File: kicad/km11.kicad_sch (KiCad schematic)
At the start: 8 parts, among them J1 DEC-FLIP-CHIP_CONN-DEC-DOUBLE, U1 ATtiny1616-S, U2 PCF8574T, U3 PCF8574T, U4 PCF8574T, U5 PCF8574T, U6 PCF8574T, U7 PCF8574T

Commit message: First small parts
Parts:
- added C1, C2, C3, C4, C5, C6, C7: 100nF, Capacitor_SMD:C_0805_2012Metric, symbol Device:C
- added C8: 100uF, Capacitor_SMD:CP_Elec_6.3x7.7, symbol Device:C_Polarized
- added J2: Conn_02x10_Odd_Even, Connector_PinHeader_2.54mm:PinHeader_2x10_P2.54mm_Vertical, symbol Connector_Generic:Conn_02x10_Odd_Even
- added R1, R2: 4.7k, Resistor_SMD:R_0805_2012Metric, symbol Device:R
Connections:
- net GND: now reaches U4.1 (A0)
- net GND: now also U1.20 (GND), U2.1 (A0), U2.2 (A1), U2.3 (A2), U2.8 (GND), U3.2 (A1), U3.3 (A2), U3.8 (GND), U4.3 (A2), U4.8 (GND), U5.3 (A2), U5.8 (GND), U6.1 (A0), U6.2 (A1), U6.8 (GND), U7.2 (A1), U7.8 (GND), C1.2, C2.2, C3.2, C4.2, C5.2, C6.2, C7.2, C8.2, J2.1 (Pin_1), J2.2 (Pin_2)
- net SCL: now reaches U4.14 (SCL)
- net SCL: now also U1.11 (PB0), U2.14 (SCL), U3.14 (SCL), U5.14 (SCL), U6.14 (SCL), U7.14 (SCL), R2.2
- net SDA: now reaches U4.15 (SDA)
- net SDA: now also U1.10 (PB1), U2.15 (SDA), U3.15 (SDA), U5.15 (SDA), U6.15 (SDA), U7.15 (SDA), R1.2
- net +5V: now reaches U4.16 (VDD)
- net +5V: now also U1.1 (VCC), U2.16 (VDD), U3.1 (A0), U3.16 (VDD), U4.2 (A1), U5.1 (A0), U5.16 (VDD), U5.2 (A1), U6.16 (VDD), U6.3 (A2), U7.1 (A0), U7.16 (VDD), U7.3 (A2), C1.1, C2.1, C3.1, C4.1, C5.1, C6.1, C7.1, C8.1, J2.19 (Pin_19), J2.20 (Pin_20), R1.1, R2.1
- net MOSI: now reaches U1.17 (PA1)
- net MOSI: now also J2.4 (Pin_4)
- net MISO: now reaches U1.18 (PA2)
- net MISO: now also J2.6 (Pin_6)
- net SCK: now reaches U1.19 (PA3)
- net SCK: now also J2.8 (Pin_8)
- net SPI_SS: now reaches U1.2 (PA4)
- net SPI_SS: now also J2.10 (Pin_10)
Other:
- note added: "Decoupling: C1=U1 C2=U2 C3=U3 C4=U4 C5=U5 C6=U6 C7=U7 - place one adjacent to each IC's VDD pin on the PCB"

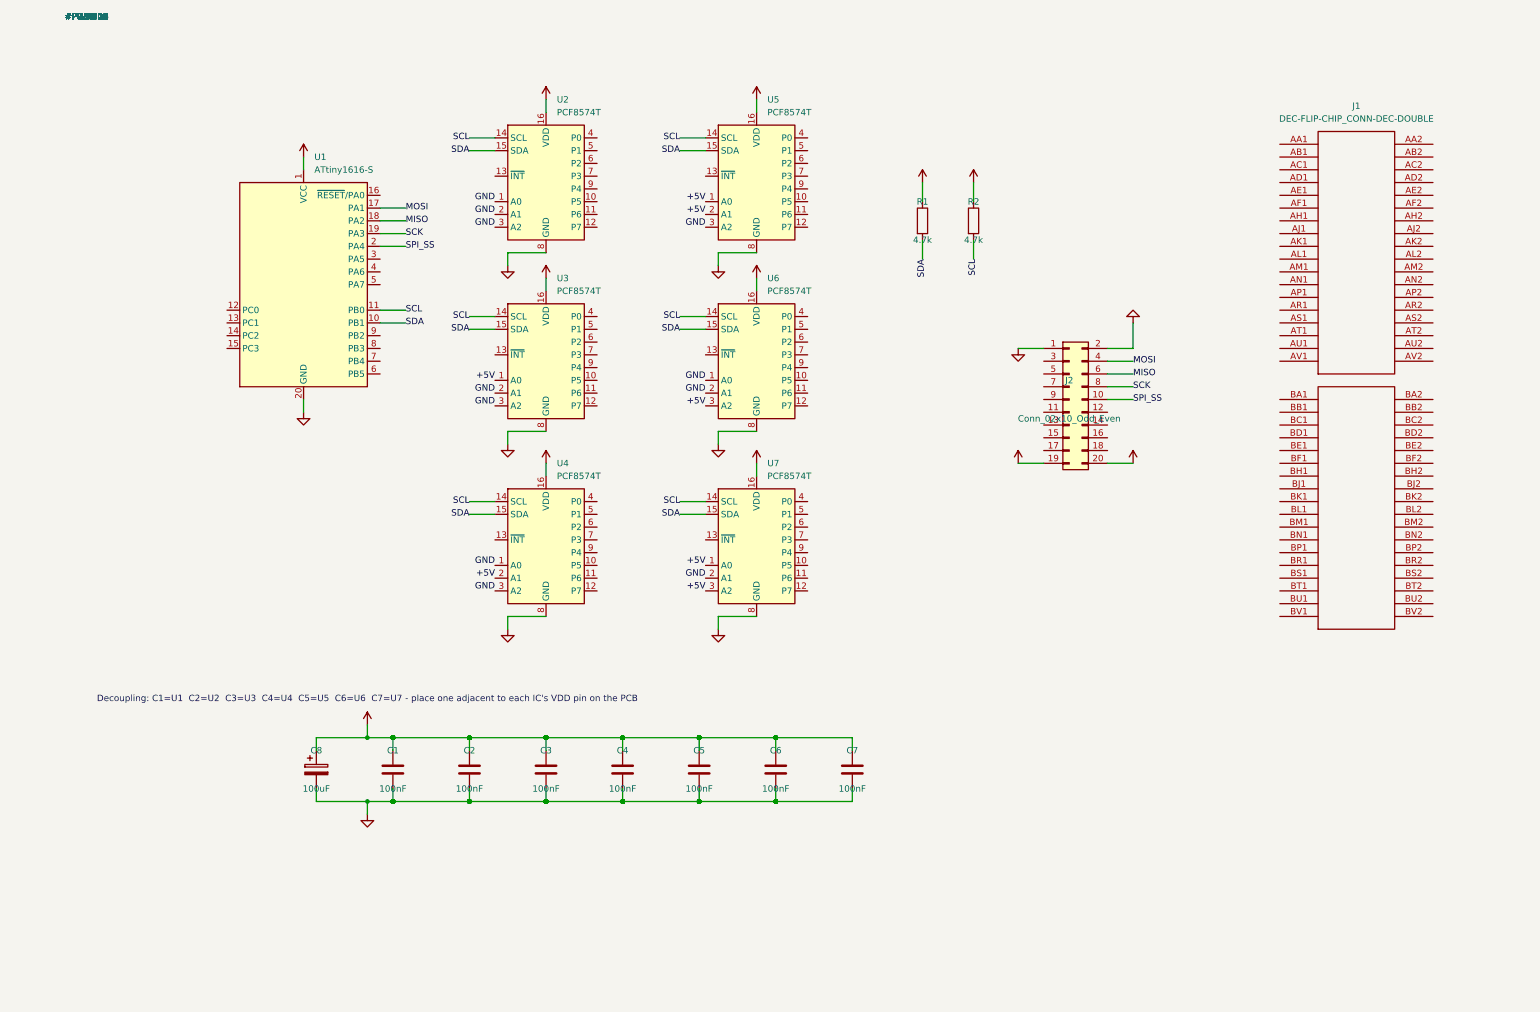
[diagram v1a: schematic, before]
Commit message: Add all flipchip signal names from Joergs sheet
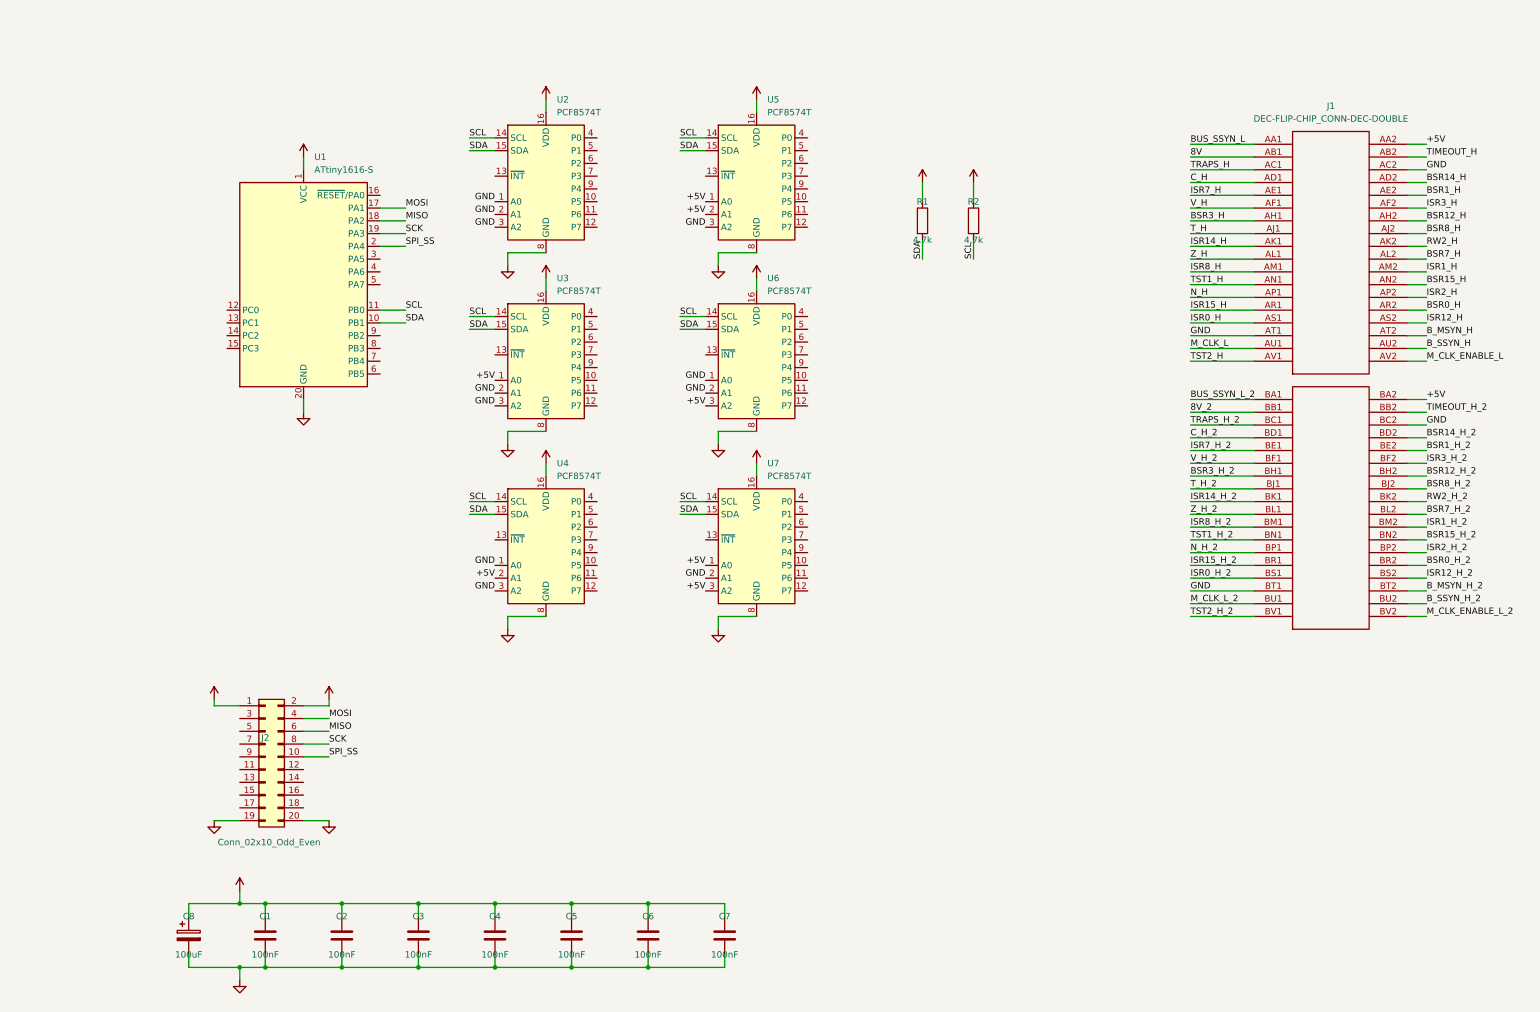
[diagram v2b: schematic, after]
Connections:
- net +5V: now also J1.AA2, J1.BA2, J2.1 (Pin_1), J2.2 (Pin_2); no longer J2.19 (Pin_19), J2.20 (Pin_20)
- net GND: now also J1.AC2, J1.AT1, J1.BC2, J1.BT1, J2.19 (Pin_19), J2.20 (Pin_20); no longer J2.1 (Pin_1), J2.2 (Pin_2)
- net BUS_SSYN_L: now reaches J1.AA1
- net 8V: now reaches J1.AB1
- net TIMEOUT_H: now reaches J1.AB2
- net TRAPS_H: now reaches J1.AC1
- net C_H: now reaches J1.AD1
- net BSR14_H: now reaches J1.AD2
- net ISR7_H: now reaches J1.AE1
- net BSR1_H: now reaches J1.AE2
- net V_H: now reaches J1.AF1
- net ISR3_H: now reaches J1.AF2
- net BSR3_H: now reaches J1.AH1
- net BSR12_H: now reaches J1.AH2
- net T_H: now reaches J1.AJ1
- net BSR8_H: now reaches J1.AJ2
- net ISR14_H: now reaches J1.AK1
- net RW2_H: now reaches J1.AK2
- net Z_H: now reaches J1.AL1
- net BSR7_H: now reaches J1.AL2
- net ISR8_H: now reaches J1.AM1
- net ISR1_H: now reaches J1.AM2
- net TST1_H: now reaches J1.AN1
- net BSR15_H: now reaches J1.AN2
- net N_H: now reaches J1.AP1
- net ISR2_H: now reaches J1.AP2
- net ISR15_H: now reaches J1.AR1
- net BSR0_H: now reaches J1.AR2
- net ISR0_H: now reaches J1.AS1
- net ISR12_H: now reaches J1.AS2
- net B_MSYN_H: now reaches J1.AT2
- net M_CLK_L: now reaches J1.AU1
- net B_SSYN_H: now reaches J1.AU2
- net TST2_H: now reaches J1.AV1
- net M_CLK_ENABLE_L: now reaches J1.AV2
- net BUS_SSYN_L_2: now reaches J1.BA1
- net 8V_2: now reaches J1.BB1
- net TIMEOUT_H_2: now reaches J1.BB2
- net TRAPS_H_2: now reaches J1.BC1
- net C_H_2: now reaches J1.BD1
- net BSR14_H_2: now reaches J1.BD2
- net ISR7_H_2: now reaches J1.BE1
- net BSR1_H_2: now reaches J1.BE2
- net V_H_2: now reaches J1.BF1
- net ISR3_H_2: now reaches J1.BF2
- net BSR3_H_2: now reaches J1.BH1
- net BSR12_H_2: now reaches J1.BH2
- net T_H_2: now reaches J1.BJ1
- net BSR8_H_2: now reaches J1.BJ2
- net ISR14_H_2: now reaches J1.BK1
- net RW2_H_2: now reaches J1.BK2
- net Z_H_2: now reaches J1.BL1
- net BSR7_H_2: now reaches J1.BL2
- net ISR8_H_2: now reaches J1.BM1
- net ISR1_H_2: now reaches J1.BM2
- net TST1_H_2: now reaches J1.BN1
- net BSR15_H_2: now reaches J1.BN2
- net N_H_2: now reaches J1.BP1
- net ISR2_H_2: now reaches J1.BP2
- net ISR15_H_2: now reaches J1.BR1
- net BSR0_H_2: now reaches J1.BR2
- net ISR0_H_2: now reaches J1.BS1
- net ISR12_H_2: now reaches J1.BS2
- net B_MSYN_H_2: now reaches J1.BT2
- net M_CLK_L_2: now reaches J1.BU1
- net B_SSYN_H_2: now reaches J1.BU2
- net TST2_H_2: now reaches J1.BV1
- net M_CLK_ENABLE_L_2: now reaches J1.BV2
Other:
- note removed: "Decoupling: C1=U1 C2=U2 C3=U3 C4=U4 C5=U5 C6=U6 C7=U7 - place one adjacent to each IC's VDD pin on the PCB"
- moved on the sheet: C1, C2, C3, C4, C5, C6, C7, C8, J1, J2

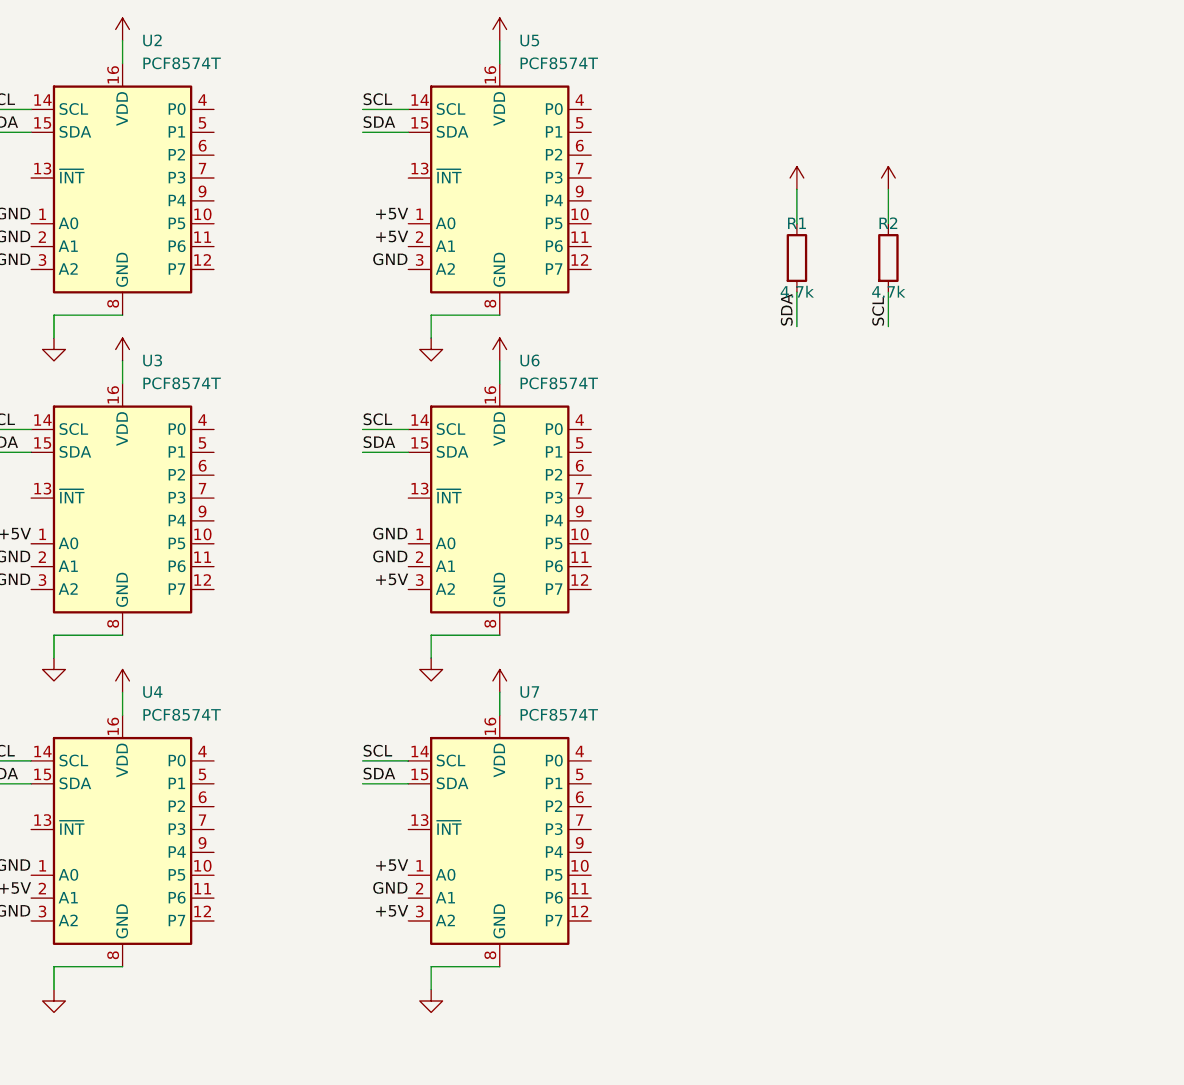
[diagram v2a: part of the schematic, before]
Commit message: All ports assigned
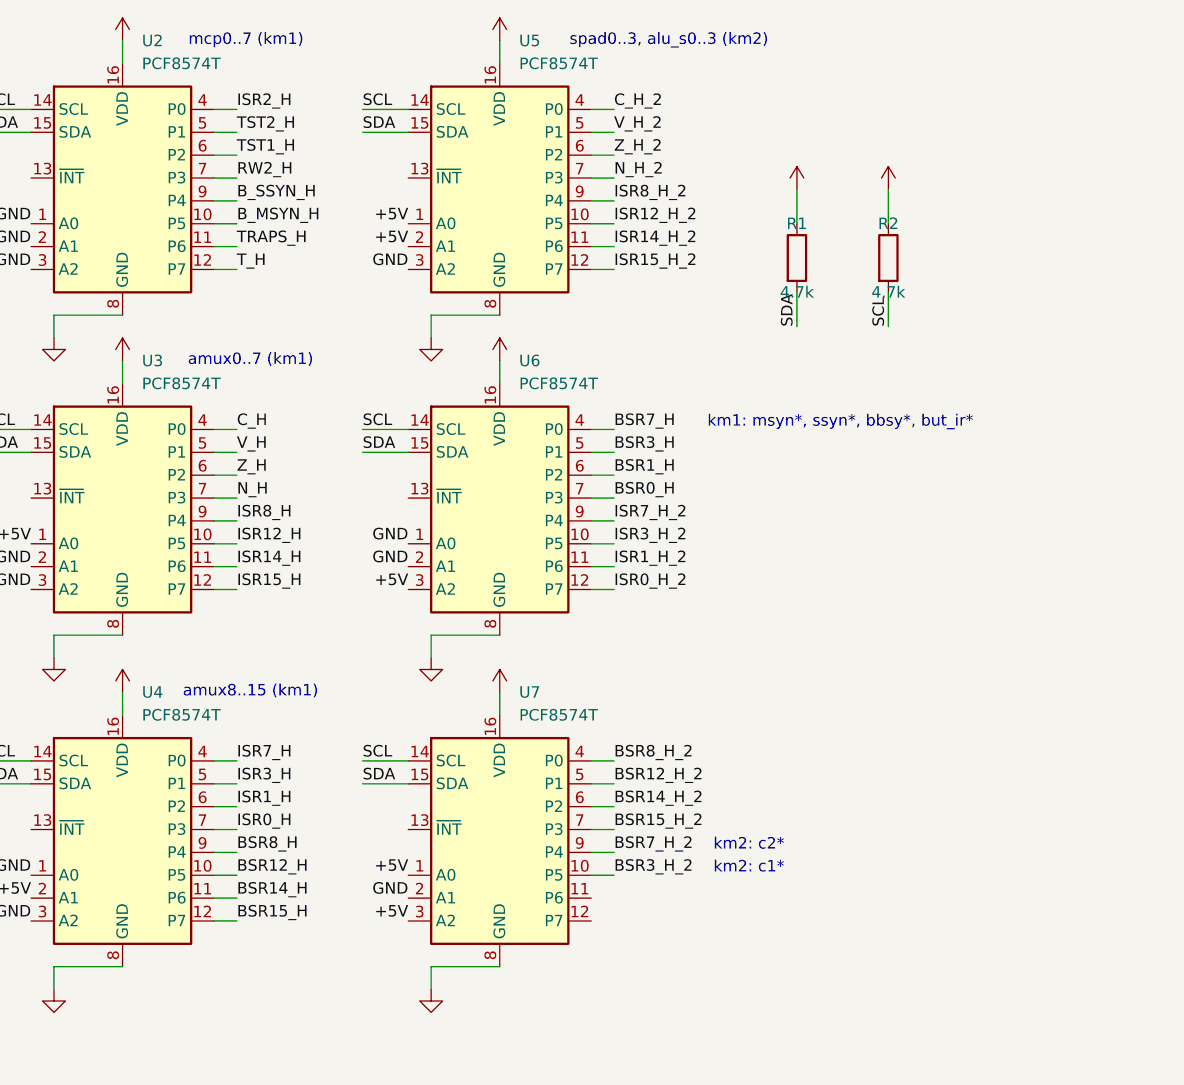
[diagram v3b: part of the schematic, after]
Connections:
- net BSR0_H: now also U6.7 (P3)
- net BSR12_H: now also U4.10 (P5)
- net BSR12_H_2: now also U7.5 (P1)
- net BSR14_H: now also U4.11 (P6)
- net BSR14_H_2: now also U7.6 (P2)
- net BSR15_H: now also U4.12 (P7)
- net BSR15_H_2: now also U7.7 (P3)
- net BSR1_H: now also U6.6 (P2)
- net BSR3_H: now also U6.5 (P1)
- net BSR3_H_2: now also U7.10 (P5)
- net BSR7_H: now also U6.4 (P0)
- net BSR7_H_2: now also U7.9 (P4)
- net BSR8_H: now also U4.9 (P4)
- net BSR8_H_2: now also U7.4 (P0)
- net B_MSYN_H: now also U2.10 (P5)
- net B_SSYN_H: now also U2.9 (P4)
- net C_H: now also U3.4 (P0)
- net C_H_2: now also U5.4 (P0)
- net ISR0_H: now also U4.7 (P3)
- net ISR0_H_2: now also U6.12 (P7)
- net ISR12_H: now also U3.10 (P5)
- net ISR12_H_2: now also U5.10 (P5)
- net ISR14_H: now also U3.11 (P6)
- net ISR14_H_2: now also U5.11 (P6)
- net ISR15_H: now also U3.12 (P7)
- net ISR15_H_2: now also U5.12 (P7)
- net ISR1_H: now also U4.6 (P2)
- net ISR1_H_2: now also U6.11 (P6)
- net ISR2_H: now also U2.4 (P0)
- net ISR3_H: now also U4.5 (P1)
- net ISR3_H_2: now also U6.10 (P5)
- net ISR7_H: now also U4.4 (P0)
- net ISR7_H_2: now also U6.9 (P4)
- net ISR8_H: now also U3.9 (P4)
- net ISR8_H_2: now also U5.9 (P4)
- net N_H: now also U3.7 (P3)
- net N_H_2: now also U5.7 (P3)
- net RW2_H: now also U2.7 (P3)
- net TRAPS_H: now also U2.11 (P6)
- net TST1_H: now also U2.6 (P2)
- net TST2_H: now also U2.5 (P1)
- net T_H: now also U2.12 (P7)
- net V_H: now also U3.5 (P1)
- net V_H_2: now also U5.5 (P1)
- net Z_H: now also U3.6 (P2)
- net Z_H_2: now also U5.6 (P2)
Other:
- note added: "amux0..7 (km1)"
- note added: "amux8..15 (km1)"
- note added: "km1: msyn*, ssyn*, bbsy*, but_ir*"
- note added: "km2: c1*"
- note added: "km2: c2*"
- note added: "mcp0..7 (km1)"
- note added: "spad0..3, alu_s0..3 (km2)"

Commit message: Initial routed
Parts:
- added C10, C11: 10uF, Capacitor_SMD:CP_Elec_8x5.4, symbol Device:C_Polarized
- added C9: 100nF, Capacitor_SMD:C_0805_2012Metric, symbol Device:C
- added D1: PWRLED, LED_SMD:LED_1206_3216Metric_Pad1.42x1.75mm_HandSolder, symbol Device:LED
- added D2: +3V_LED, LED_SMD:LED_1206_3216Metric_Pad1.42x1.75mm_HandSolder, symbol Device:LED
- added J3: pgm_hdr, Connector_PinHeader_2.54mm:PinHeader_1x03_P2.54mm_Vertical, symbol Connector_Generic:Conn_01x03
- added JP1: Jumper_2_Bridged, Jumper:SolderJumper-2_P1.3mm_Bridged_RoundedPad1.0x1.5mm, symbol Jumper:Jumper_2_Bridged
- added Q1: BC547, Package_TO_SOT_THT:TO-92_Inline, symbol Transistor_BJT:BC547
- added R10, R11, R4, R5, R6, R7, R8, R9: 1K, Resistor_SMD:R_0805_2012Metric, symbol Device:R
- added U8: 74ACT00SC, Package_SO:SOIC-14W_7.5x9mm_P1.27mm, symbol 74xx:74LS00
- added U9: LD1117S33TR_SOT223, Package_TO_SOT_SMD:SOT-223-3_TabPin2, symbol Regulator_Linear:LD1117S33TR_SOT223
- J2: value Conn_02x10_Odd_Even -> display_switches_hdr
- renumbered J1 to J9
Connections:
- net +5V: now also C10.1, C9.1, J3.3 (Pin_3), R10.1, R4.1, R6.1, R7.1, R8.1, R9.1, U8.14 (VCC), U9.3 (VI)
- net BUS_SSYN_L: now also Q1.1 (C)
- net GND: now also C10.2, C11.2, C9.2, D1.1 (K), D2.1 (K), J3.1 (Pin_1), Q1.3 (E), U8.7 (GND), U9.1 (GND)
- net M_CLK_ENABLE_L: now also J2.5 (Pin_5), R4.2
- net M_CLK_L: now also JP1.2 (B)
- net TIMEOUT_H: now also J2.3 (Pin_3)
- net ~{RESET}PA0: now reaches U1.16 (~{RESET}/PA0)
- net ~{RESET}PA0: now also J3.2 (Pin_2)
- net PB5: now reaches U1.6 (PB5)
- net PB5: now also J2.18 (Pin_18)
- net PB4: now reaches U1.7 (PB4)
- net PB4: now also J2.16 (Pin_16)
- net PB3: now reaches U1.8 (PB3)
- net PB3: now also J2.14 (Pin_14)
- net PB2: now reaches U1.9 (PB2)
- net PB2: now also J2.12 (Pin_12)
- net s4_off: now reaches J2.11 (Pin_11)
- net s4_off: now also R7.2, U8.9
- net s4_on: now reaches J2.13 (Pin_13)
- net s4_on: now also R9.2, U8.13
- net +3.3V: now reaches J2.15 (Pin_15)
- net +3.3V: now also J2.17 (Pin_17), C11.1, R11.1, U9.2 (VO)
- net s3_off: now reaches J2.7 (Pin_7)
- net s3_off: now also R6.2, U8.1
- net s3_on: now reaches J2.9 (Pin_9)
- net s3_on: now also R8.2, U8.5
- new net: U8.10, U8.11
- new net: JP1.1 (A), U8.12, U8.8
- new net: D1.2 (A), R10.2
- new net: R5.1, U8.2, U8.6
- new net: Q1.2 (B), R5.2
- new net: D2.2 (A), R11.2
- new net: U8.3, U8.4
- no-connect marks 0 -> 15
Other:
- moved on the sheet: C1, C2, C3, C4, C5, C6, C7, J2
